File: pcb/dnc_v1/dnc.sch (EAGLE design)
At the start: 127 parts, among them IC1 LM2596S, IC2 74S244DW, Q1 IRF9321PBF, Q10 BSS316, Q11 BSS316, Q12 BSS138, Q2 BSS670, Q3 BSS138, Q4 BSS670, Q5 BSS138, Q6 BSS670, Q7 BSS138, Q8 BSS138, Q9 BSS670, U1 MAX202CDWR, U2 74HCT595D, U3 TC7SU04F, U4 AL8807, U5 AL8807, U6 TC7SU04F

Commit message: maj 22 janv
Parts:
- removed D3: 33v, SparkFun-DiscreteSemi:DIODE-ZENERSOD-123
- added Q13: BSS138, SparkFun-DiscreteSemi:MOSFET-NCHANNELBSS138
- added R44: 10K, SparkFun-Passives:RESISTOR0603-RES
- added TVS: TVS-30V, SparkFun:TVS
- added U$1: RADIATEUR, pierre_vv:RADIATEUR
- added U$2: LOGO, pierre_vv:LOGO
- C2: value (none) -> 220u
- L1: value 100nH -> 68nH3A
- LG, LR: device led:LEDCHIPLED_0603 -> SparkFun-LED:LED1206
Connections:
- new net CHARGING: JP1.2, U$4.GPIO23
- new net RELAY_CHARGE_BOARD: JP1.1, U$4.GPIO24
- new net RESET_5V: AT328.PC6(/RESET), C26.2, ISP.5, Q13.D, R21.1
- net +3V3: now also Q13.G, R44.2
- net GND: now also TVS.1; no longer D3.A, JP1.2
- net RAW_POL_PROTECTED: now also TVS.2; no longer D3.C
- net RAW_UNPROTECTED: no longer JP1.1
- net RESET: now also Q13.S, R44.1, U$4.GPIO27; no longer AT328.PC6(/RESET), C26.2, ISP.5, R21.1
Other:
- moved on the sheet: IC1

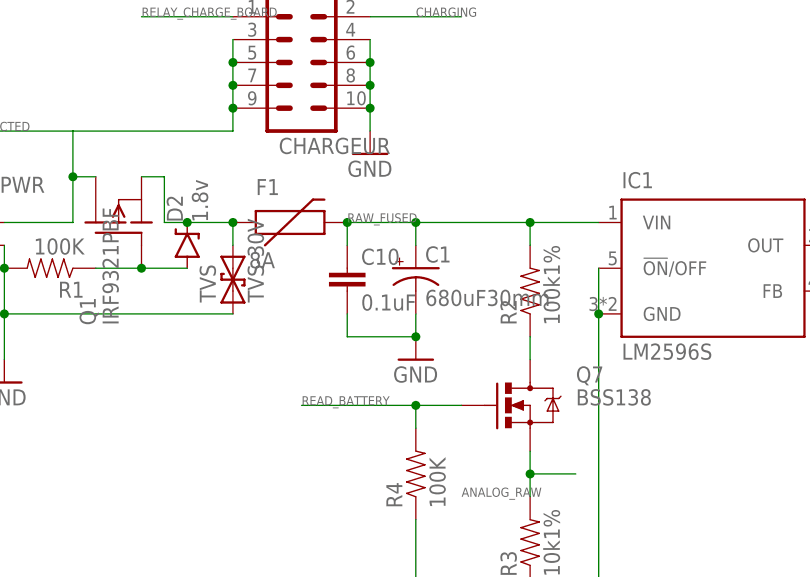
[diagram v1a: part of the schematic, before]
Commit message: carte extension chargeur LIPO
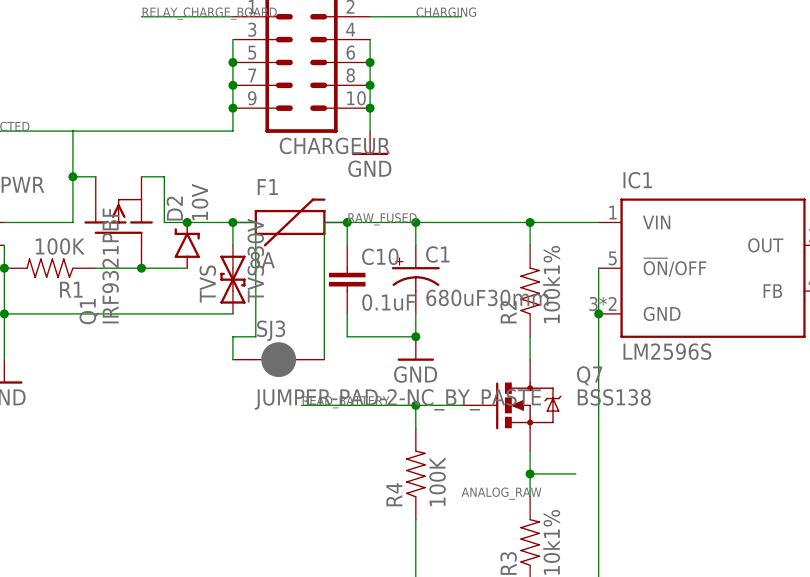
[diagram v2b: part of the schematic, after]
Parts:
- added SJ3: JUMPER-PAD-2-NC_BY_PASTE, SparkFun-Passives:JUMPER-PAD-2-NC_BY_PASTE
- D2: value 1.8v -> 10V
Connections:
- net RAW_FUSED: now also SJ3.2
- net RAW_POL_PROTECTED: now also SJ3.1
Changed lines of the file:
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@@
 <part name="C10" library="rcl" deviceset="C-EU" device="C0603" value="0.1uF"/>
 <part name="C11" library="rcl" deviceset="C-EU" device="C0603" value="0.1uF"/>
-<part name="D2" library="SparkFun-DiscreteSemi" deviceset="DIODE-ZENER" device="SOD-123" value="1.8v"/>
+<part name="D2" library="SparkFun-DiscreteSemi" deviceset="DIODE-ZENER" device="SOD-123" value="10V"/>
 <part name="R1" library="SparkFun-Passives" deviceset="RESISTOR" device="0603-RES" value="100K"/>
 <part name="Q1" library="pierre_vv" deviceset="IRF9321PBF" device=""/>
@@
 <part name="R44" library="SparkFun-Passives" deviceset="RESISTOR" device="0603-RES" value="10K"/>
 <part name="P+24" library="supply1" deviceset="+5V" device=""/>
+<part name="SJ3" library="SparkFun-Passives" deviceset="JUMPER-PAD-2-NC_BY_PASTE" device=""/>
 </parts>
 <sheets>
@@
 <instance part="R44" gate="G$1" x="160.02" y="116.84" rot="R90"/>
 <instance part="P+24" gate="1" x="129.54" y="134.62"/>
+<instance part="SJ3" gate="G$1" x="45.72" y="210.82"/>
 </instances>
 <busses>
@@
 <pinref part="F1" gate="G$1" pin="2"/>
 <junction x="53.34" y="226.06"/>
+<pinref part="SJ3" gate="G$1" pin="2"/>
+<wire x1="50.8" y1="210.82" x2="50.8" y2="226.06" width="0.1524" layer="91"/>
+<wire x1="50.8" y1="226.06" x2="53.34" y2="226.06" width="0.1524" layer="91"/>
 </segment>
 <segment>
@@
 <wire x1="40.64" y1="226.06" x2="40.64" y2="223.52" width="0.1524" layer="91"/>
 <junction x="40.64" y="226.06"/>
-</segment>
-</net>
+<wire x1="40.64" y1="226.06" x2="43.18" y2="226.06" width="0.1524" layer="91"/>
+<wire x1="43.18" y1="226.06" x2="43.18" y2="213.36" width="0.1524" layer="91"/>
+<pinref part="SJ3" gate="G$1" pin="1"/>
+<wire x1="43.18" y1="213.36" x2="40.64" y2="213.36" width="0.1524" layer="91"/>
+<wire x1="40.64" y1="213.36" x2="40.64" y2="210.82" width="0.1524" layer="91"/>
+</segment>
+</net>

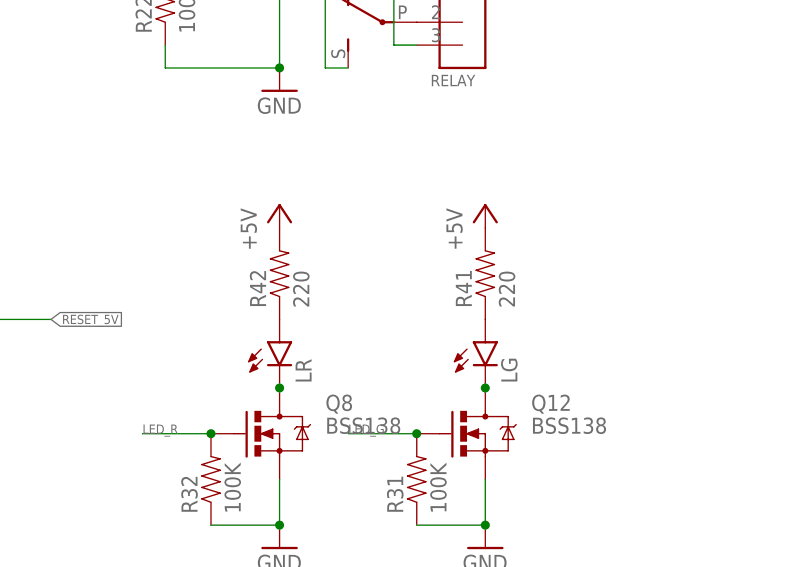
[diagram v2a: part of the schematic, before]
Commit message: add remote + enclosure
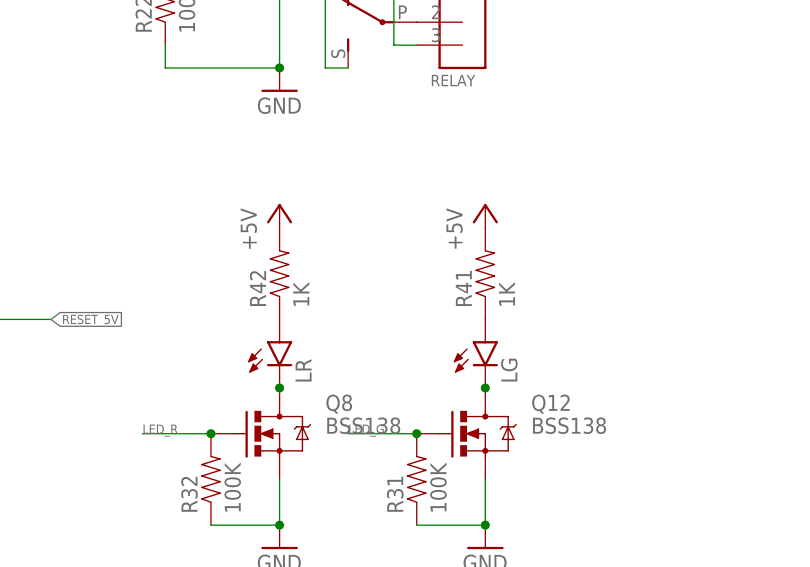
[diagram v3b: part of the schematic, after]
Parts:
- R41, R42: value 220 -> 1K
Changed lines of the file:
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@@
 <part name="GND7" library="SparkFun" deviceset="GND" device=""/>
 <part name="LR" library="SparkFun-LED" deviceset="LED" device="1206"/>
-<part name="R42" library="SparkFun-Passives" deviceset="RESISTOR" device="0603-RES" value="220"/>
+<part name="R42" library="SparkFun-Passives" deviceset="RESISTOR" device="0603-RES" value="1K"/>
 <part name="P+8" library="supply1" deviceset="+5V" device=""/>
 <part name="Q12" library="SparkFun-DiscreteSemi" deviceset="MOSFET-NCHANNEL" device="BSS138" value="BSS138"/>
@@
 <part name="GND9" library="SparkFun" deviceset="GND" device=""/>
 <part name="LG" library="SparkFun-LED" deviceset="LED" device="1206"/>
-<part name="R41" library="SparkFun-Passives" deviceset="RESISTOR" device="0603-RES" value="220"/>
+<part name="R41" library="SparkFun-Passives" deviceset="RESISTOR" device="0603-RES" value="1K"/>
 <part name="P+9" library="supply1" deviceset="+5V" device=""/>
 <part name="U$6" library="pierre_vv" deviceset="M08" device=""/>

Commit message: BOM + carte insa
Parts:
- 16MHZ: OC_FARNELL (none) -> 2101363
- A+_UART, ISP, JP1, JP13, JP14, JP19, JP2, JP3, JP4, JP5, PROG1, RAW_IN, RS232, SJ1, SJ2, SJ3, TITREUR1, TITREUR2, U$2, U$4: MOUNT (none) -> NO
- AT328: OC_FARNELL (none) -> 2443176
- C1: MOUNT (none) -> NO; OC_FARNELL (none) -> 1800687
- C2: OC_FARNELL (none) -> 2326175RL
- D1, D4, D5: OC_FARNELL (none) -> 1861427
- D2: OC_FARNELL (none) -> 1431256
- D6: OC_FARNELL (none) -> 9843841RL
- EXT1: value EXT1 -> EXT; MOUNT (none) -> NO
- EXT2: value EXT2 -> EXT; MOUNT (none) -> NO
- F1: MOUNT (none) -> NO; OC_FARNELL (none) -> 1861144
- FLEX: value FLEX -> PLUG-3; MOUNT (none) -> NO
- GYRO-LED: value GYRO LED -> PLUG-6; MOUNT (none) -> NO
- IC1: OC_FARNELL (none) -> 1469194
- IC2: value 74S244DW -> 74ACT244SC; OC_FARNELL (none) -> 1014150
- INPUT: value M08 -> PLUG-8; MOUNT (none) -> NO
- L1: OC_FARNELL (none) -> 2288510
- L2, L3: value 100nH -> 100nH2.4A; OC_FARNELL (none) -> 1864459RL
- LED10W1: value LED10W1 -> PLUG-2; MOUNT (none) -> NO
- LED10W2: value LED10W2 -> PLUG-2; MOUNT (none) -> NO
- LG: OC_FARNELL (none) -> 2426223
- LR: OC_FARNELL (none) -> 2426229
- Q10, Q11: device SparkFun-DiscreteSemi:MOSFET-NCHANNELBSS138 -> SparkFun-DiscreteSemi:MOSFET-NCHANNELBSS316
- Q2, Q4, Q6, Q9: device SparkFun-DiscreteSemi:MOSFET-NCHANNELBSS138 -> SparkFun-DiscreteSemi:MOSFET-NCHANNELBSS670
- R12: value (none) -> 5.1K
- RELAY: value RELAY -> PLUG-3; MOUNT (none) -> NO
- RELAY1: MOUNT (none) -> NO; OC_FARNELL (none) -> 2213788
- S1: OC_FARNELL (none) -> 2079502
- TVS: OC_FARNELL (none) -> 9802819RL
- U$1: MOUNT (none) -> NO; OC_FARNELL (none) -> 1703172
- U$8: MOUNT (none) -> NO; OC_FARNELL (none) -> 1849917
- U1: OC_FARNELL (none) -> 2382871
- U2: OC_FARNELL (none) -> 2445164
- U3, U6: OC_FARNELL (none) -> 1105925
- U4, U5: value AL8807 -> AL8805WS
- renumbered PLUG_3.81_1 to FLEX, PLUG_3.81_2 to RELAY, PLUG_3.81_2_1 to LED10W2, PLUG_3.81_2_2 to LED10W1, PLUG_3.81_6_1 to GYRO-LED, U$6 to INPUT

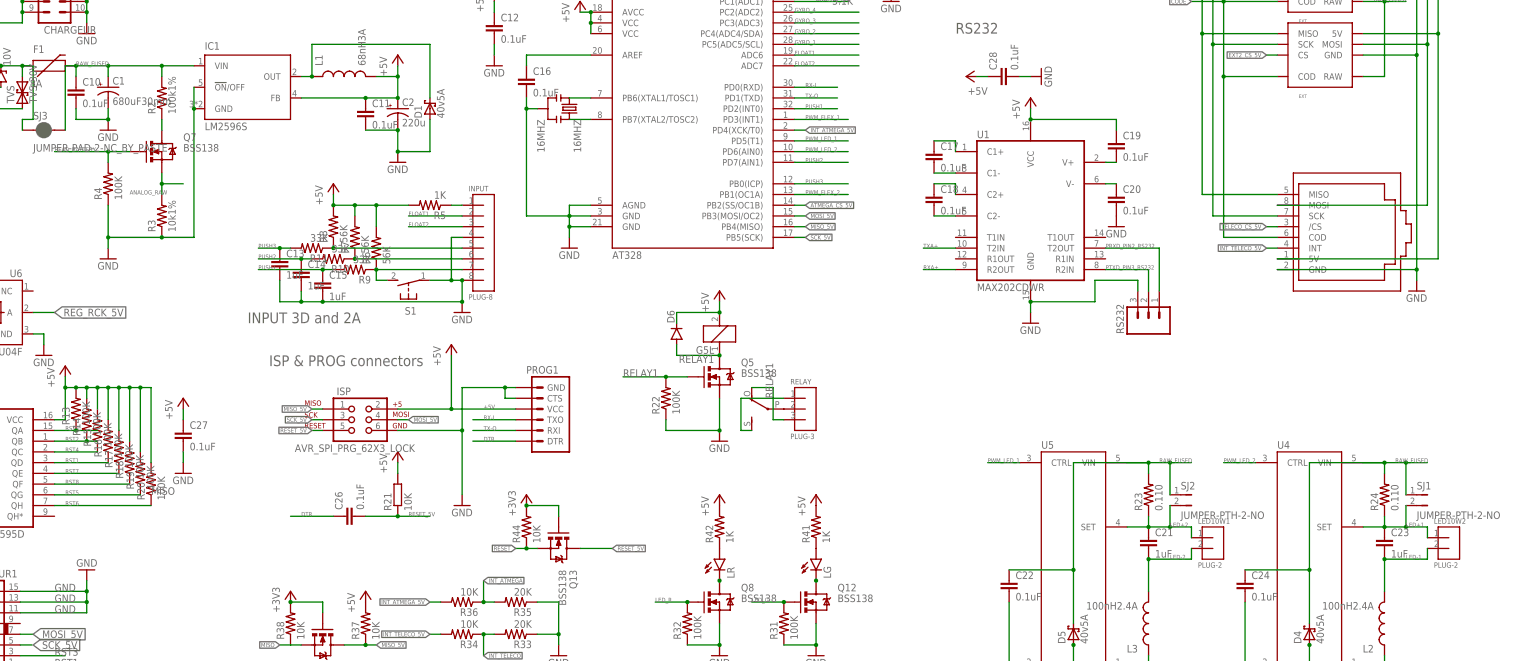
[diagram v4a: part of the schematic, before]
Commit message: minor debug (hole + value)
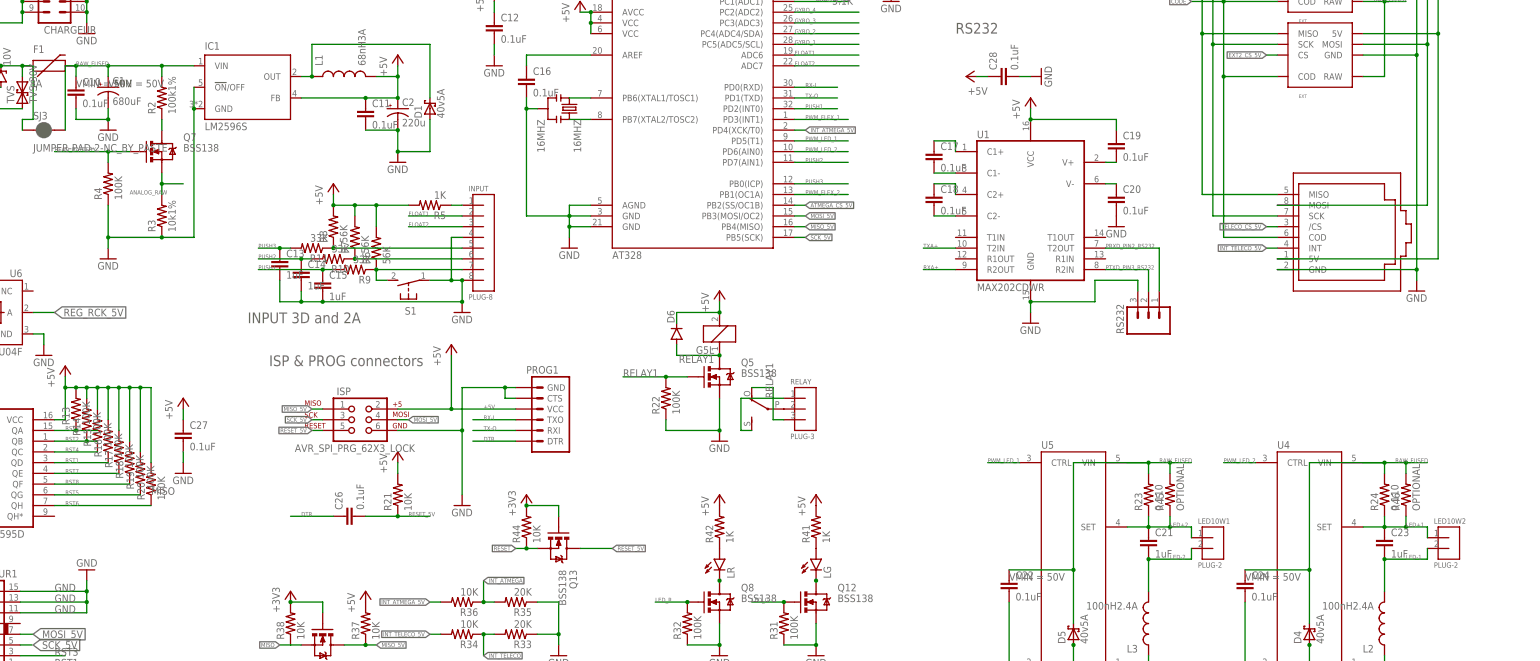
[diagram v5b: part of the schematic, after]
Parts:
- removed SJ1, SJ2: JUMPER-PTH-2-NO, SparkFun-Passives:JUMPER-PTH-2-NO
- added R45, R46: OPTIONAL, rcl:R-US_0204/2V
- C1: value 680uF30mm -> 680uF; VMIN (none) -> 50V
- C10, C22, C24: VMIN (none) -> 50V
- D6: OC_FARNELL 9843841RL -> 2101190
- R21: device rcl:R-EU_R0603 -> SparkFun-Passives:RESISTOR0603-RES
- R23, R24: device SparkFun-Passives:RESISTOR0603-RES -> SparkFun-Passives:RESISTOR0805-RES
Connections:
- net LED+1: now also R46.1; no longer SJ1.2
- net LED+2: now also R45.1; no longer SJ2.2
- net RAW_FUSED: now also R45.2, R46.2; no longer SJ1.1, SJ2.1

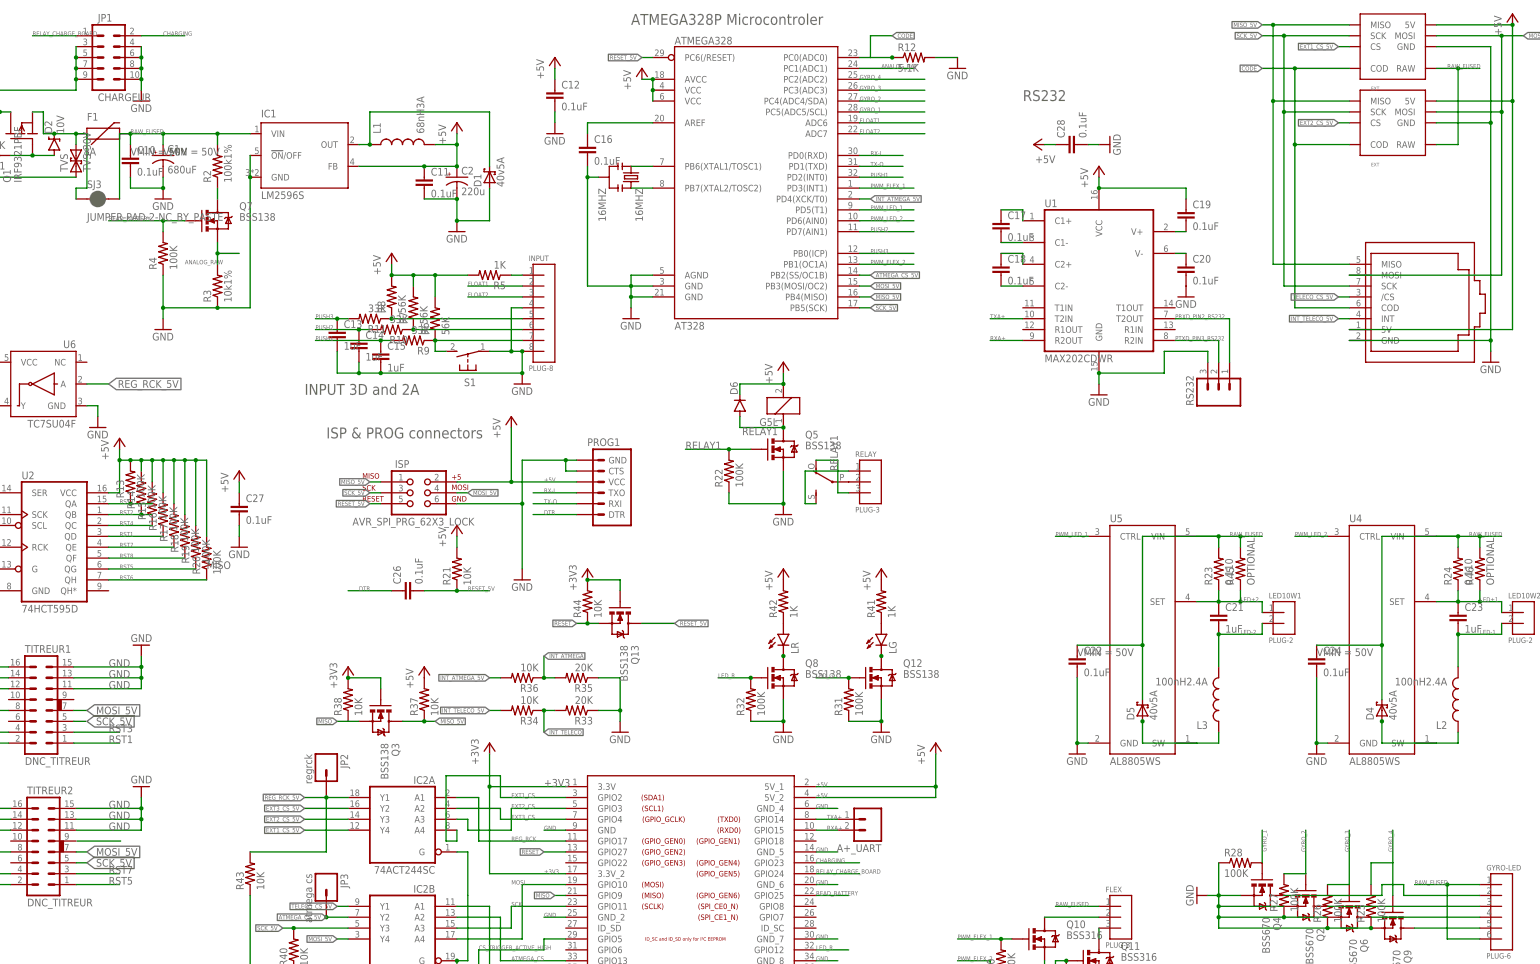
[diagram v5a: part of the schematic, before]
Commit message: major change correction : - driver led position - add usb for power - correct max 202 voltage problem - titrer connector position - forget line - power trace consideration
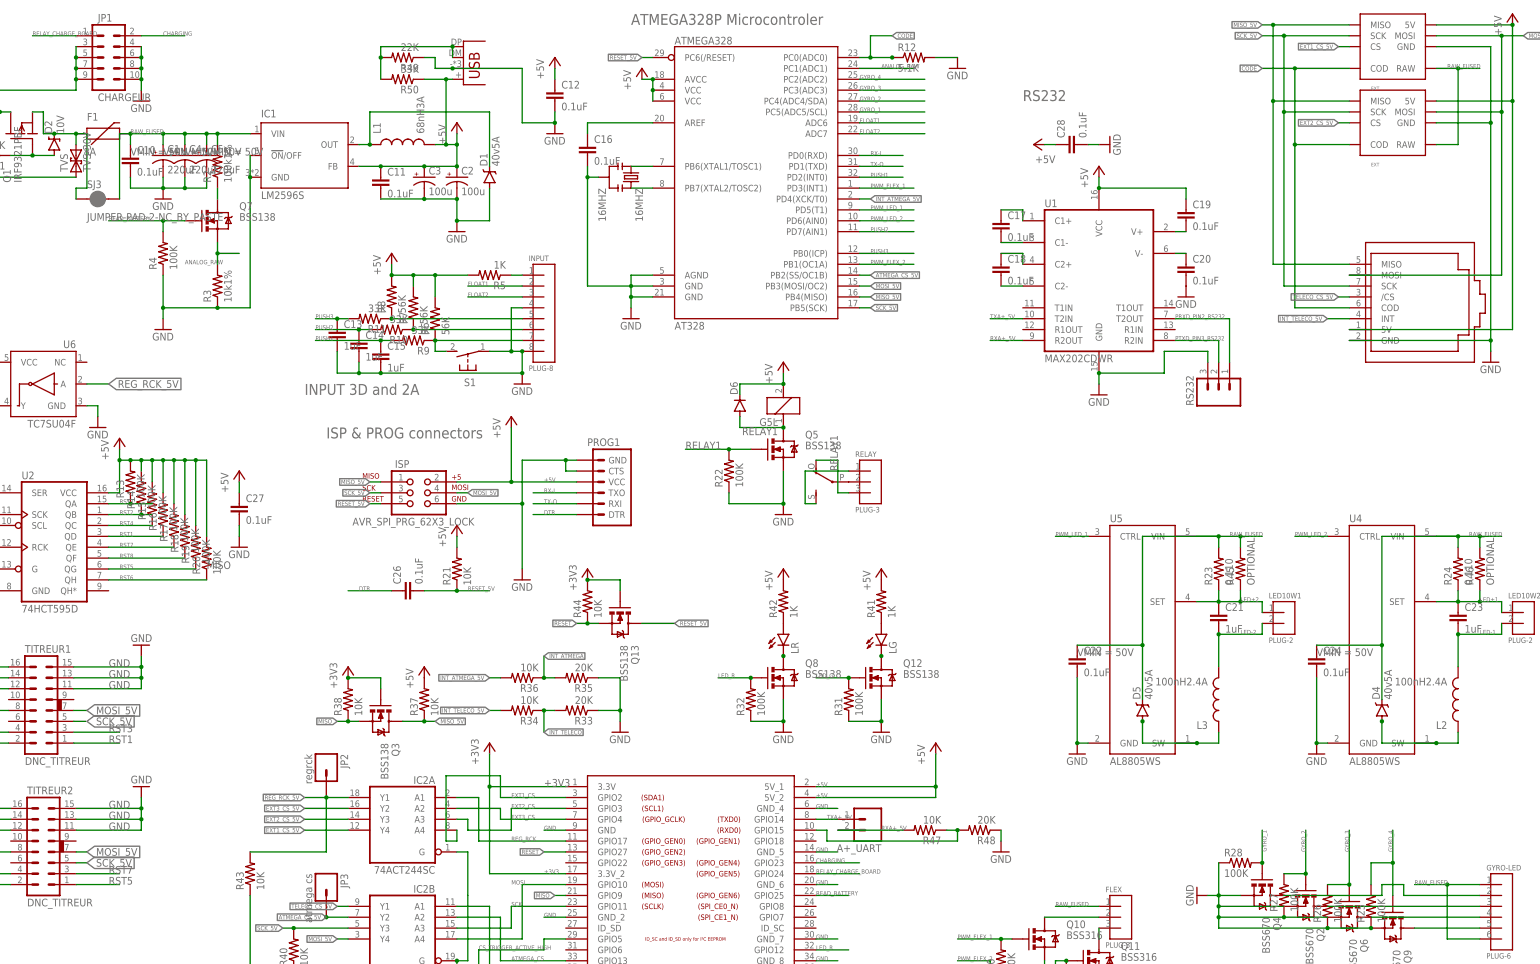
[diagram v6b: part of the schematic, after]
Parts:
- added C3: 100u, rcl:CPOL-USD
- added C4, C5: 220uF, SparkFun:CAP_POLE
- added R47: 10K, SparkFun-Passives:RESISTOR0603-RES
- added R48: 20K, SparkFun-Passives:RESISTOR0603-RES
- added R49: 22K, SparkFun-Passives:RESISTOR0603-RES
- added R50: 33K, SparkFun-Passives:RESISTOR0603-RES
- added X1: USB, pierre_vv:USB
- C1: value 680uF -> 220uF; device SparkFun:CAP_POLPTH4 -> SparkFun:CAP_POLE
- C2: value 220u -> 100u; device rcl:CPOL-USE -> rcl:CPOL-USD
- D1, D4, D5: device diode:SCHOTTKY-DIODESMC -> pierre_vv:DIODE_SCHOTKYSMPA
- JP1: device SparkFun:M05X2SHD_LOCK -> pierre_vv:M05X2
- R23, R24: device SparkFun-Passives:RESISTOR0805-RES -> rcl:R-US_R0805
- R45, R46: device rcl:R-US_0204/2V -> rcl:R-US_R0805
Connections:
- net TXA+ renamed TXA+_5V
- removed net ANALOG_BAT: AT328.PC1(ADC1)
- new net N$26: R49.2, R50.2, X1.D+, X1.D-
- new net RXA+_5V: A+_UART.2, R47.2, U1.R2OUT
- net +5V: now also C3.+, R50.1, X1.V+
- net ANALOG_RAW: now also AT328.PC1(ADC1)
- net GND: now also C3.-, C4.-, C5.-, R48.1, R49.1, X1.GND
- net RAW_FUSED: now also C4.+, C5.+
- net RXA+: now also R47.1, R48.2; no longer A+_UART.2, U1.R2OUT
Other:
- moved on the sheet: C11
